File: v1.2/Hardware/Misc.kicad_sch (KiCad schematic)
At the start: 24 parts, among them J4 DS1069-02MVW6X, J6 DS1069-04MVW6X, J7 DS1069-02MVW6X, J8 DS1069-04MVW6X, Q18 MMBT3904, Q19 MMBT3904, Q20 MMBT3904, U15 4N25, U16 ADM2483xRW

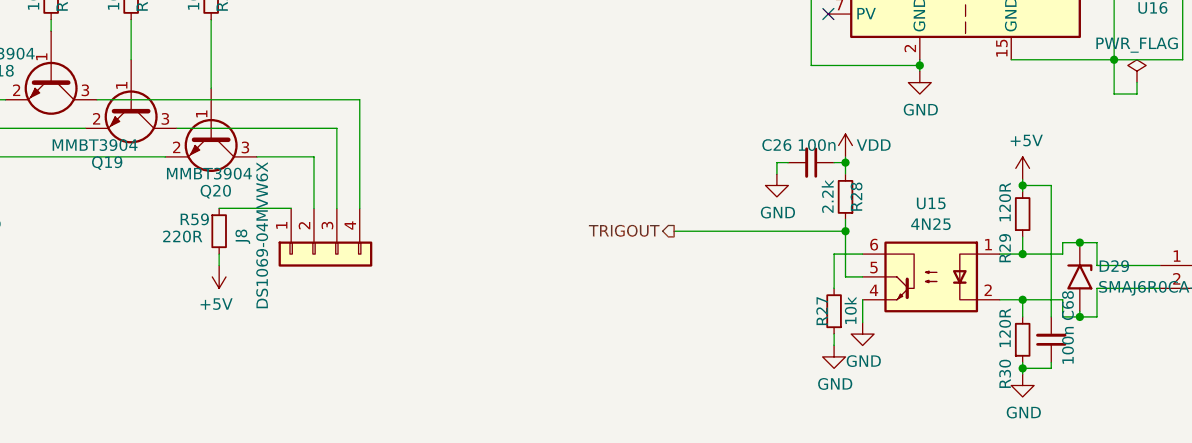
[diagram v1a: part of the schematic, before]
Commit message: Start of rs485 communication interface development.
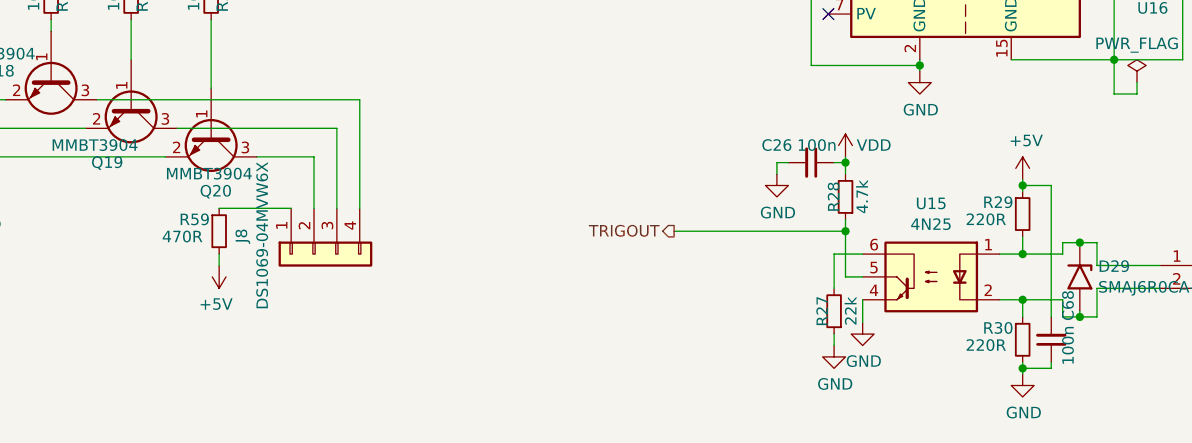
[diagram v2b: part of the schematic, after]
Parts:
- R27: value 10k -> 22k; Link https://ozdisan.com/passive-components/resistors/smt-smd-and-chip-resistors/0805S8J0103T5E -> https://ozdisan.com/passive-components/resistors/smt-smd-and-chip-resistors/0805S8J0223TDE; Price 0.01518TL -> 0.01877TL
- R28: value 2.2k -> 4.7k; Link https://ozdisan.com/passive-components/resistors/smt-smd-and-chip-resistors/0805S8J0222T5E -> https://ozdisan.com/passive-components/resistors/smt-smd-and-chip-resistors/0805S8F4701T5E; Price 0.01504TL -> 0.01955TL
- R29, R30: value 120R -> 220R; Link https://ozdisan.com/passive-components/resistors/smt-smd-and-chip-resistors/0805S8J0121T5E -> https://ozdisan.com/passive-components/resistors/smt-smd-and-chip-resistors/0805S8J0221T5E; Price 0.01492TL -> 0.01498TL
- R59: value 220R -> 470R; Link https://ozdisan.com/passive-components/resistors/smt-smd-and-chip-resistors/0805S8J0221T5E -> https://ozdisan.com/passive-components/resistors/smt-smd-and-chip-resistors/0805S8J0471T5E; Price 0.01498TL -> 0.01518TL
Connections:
- net +5V: now also R29.1; no longer R29.2
- net GND: now also R30.2; no longer R30.1
- net at D29.1 (A1), J7.1 (Pin_1), U15.1: now also R29.2; no longer R29.1
- net at D29.2 (A2), J7.2 (Pin_2), U15.2: now also R30.1; no longer R30.2

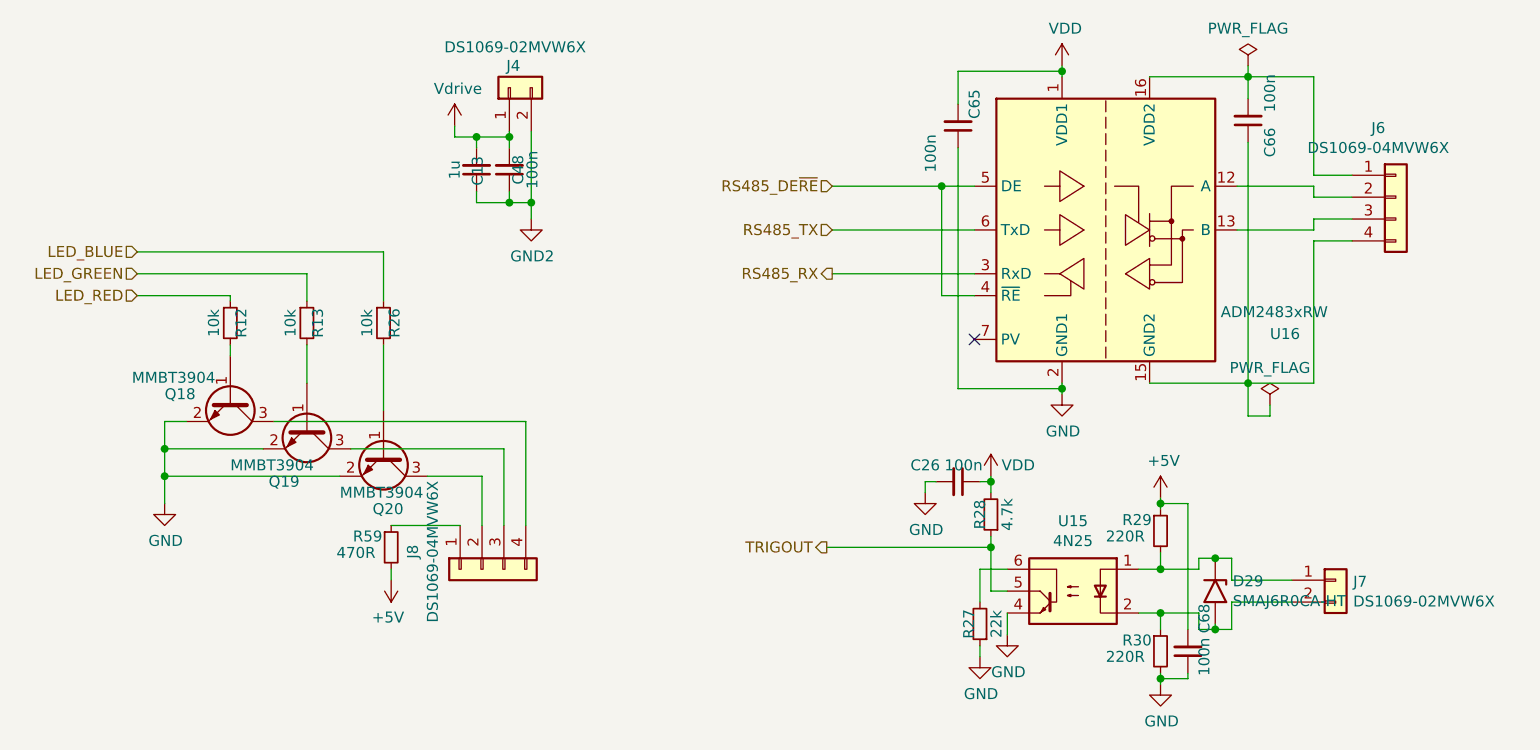
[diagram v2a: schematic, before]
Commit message: Redesign.
+Cli interface.
+Modularity improvement(complex number and pid modules created)
+Range change.
+Core-Lattice seperated. 
+Improvement of the control function
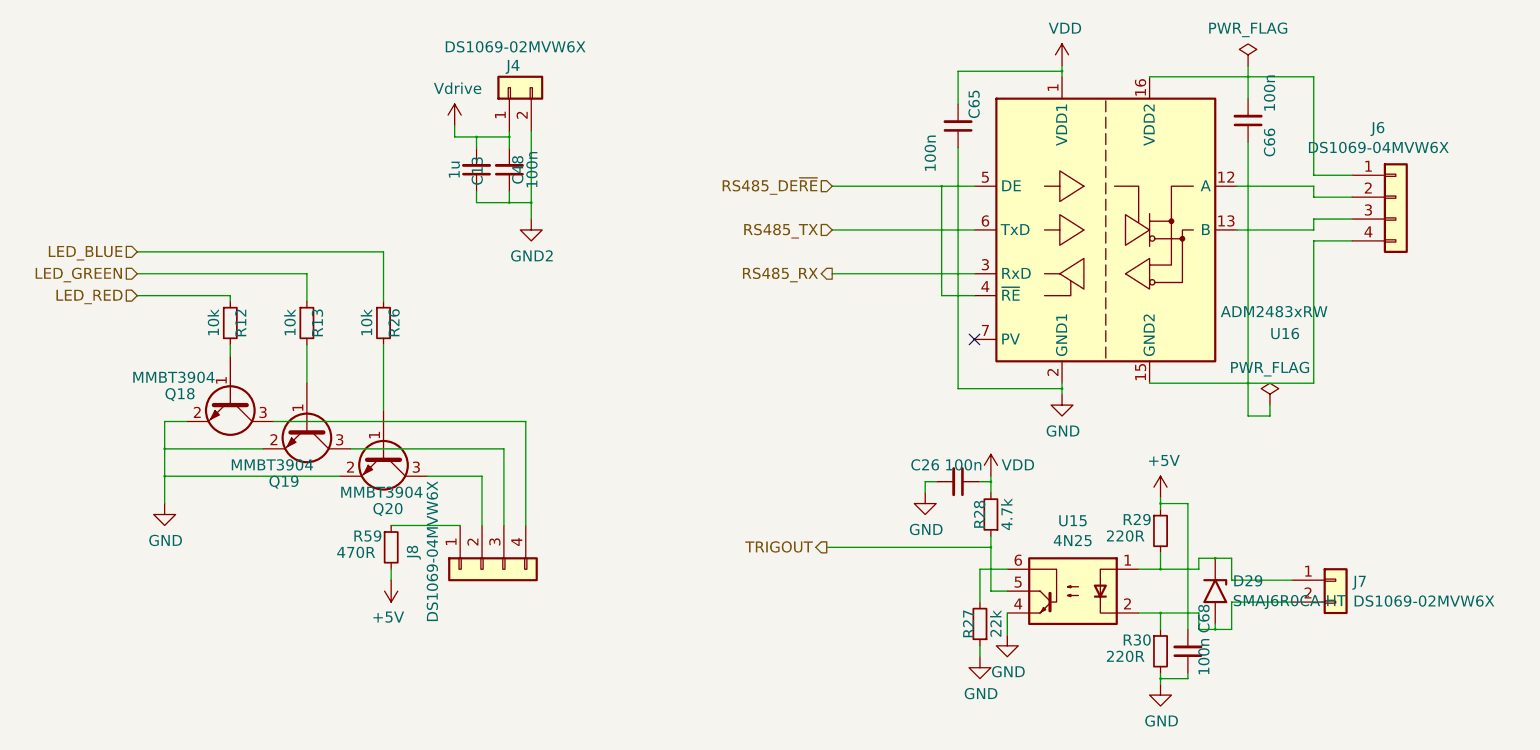
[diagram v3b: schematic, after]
